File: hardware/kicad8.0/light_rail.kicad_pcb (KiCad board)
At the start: 4 copper layers, 73.4 x 100.5 mm, 215 parts, among them J1 USB_C_Receptacle_USB2.0_16P, J2 Conn_01x04_Pin, J3 AVR-ISP-6, SW1 SW_Push, SW10 SW_Push, SW11 SW_Push, SW12 SW_Push, SW13 SW_Push, SW14 SW_SPST, SW2 SW_Push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

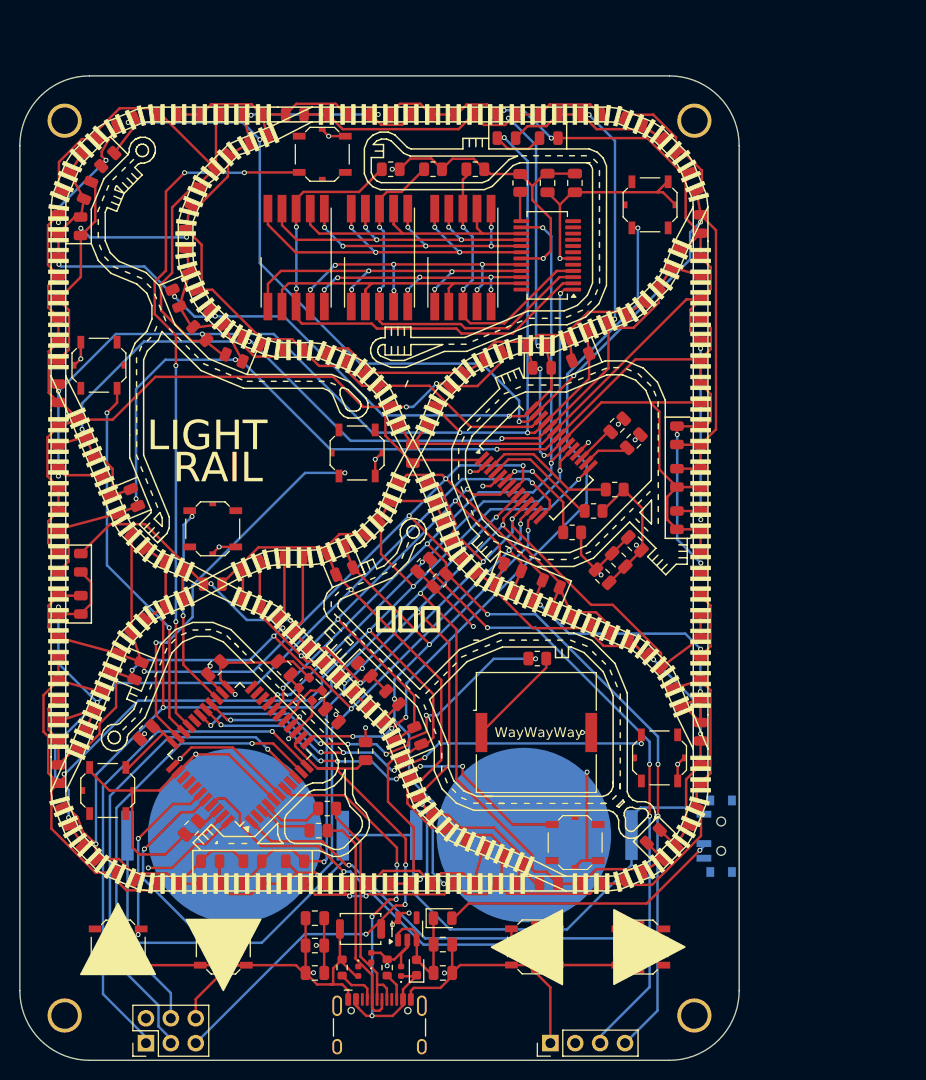
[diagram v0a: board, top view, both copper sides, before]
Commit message: added design comments to schematic, added schematic image
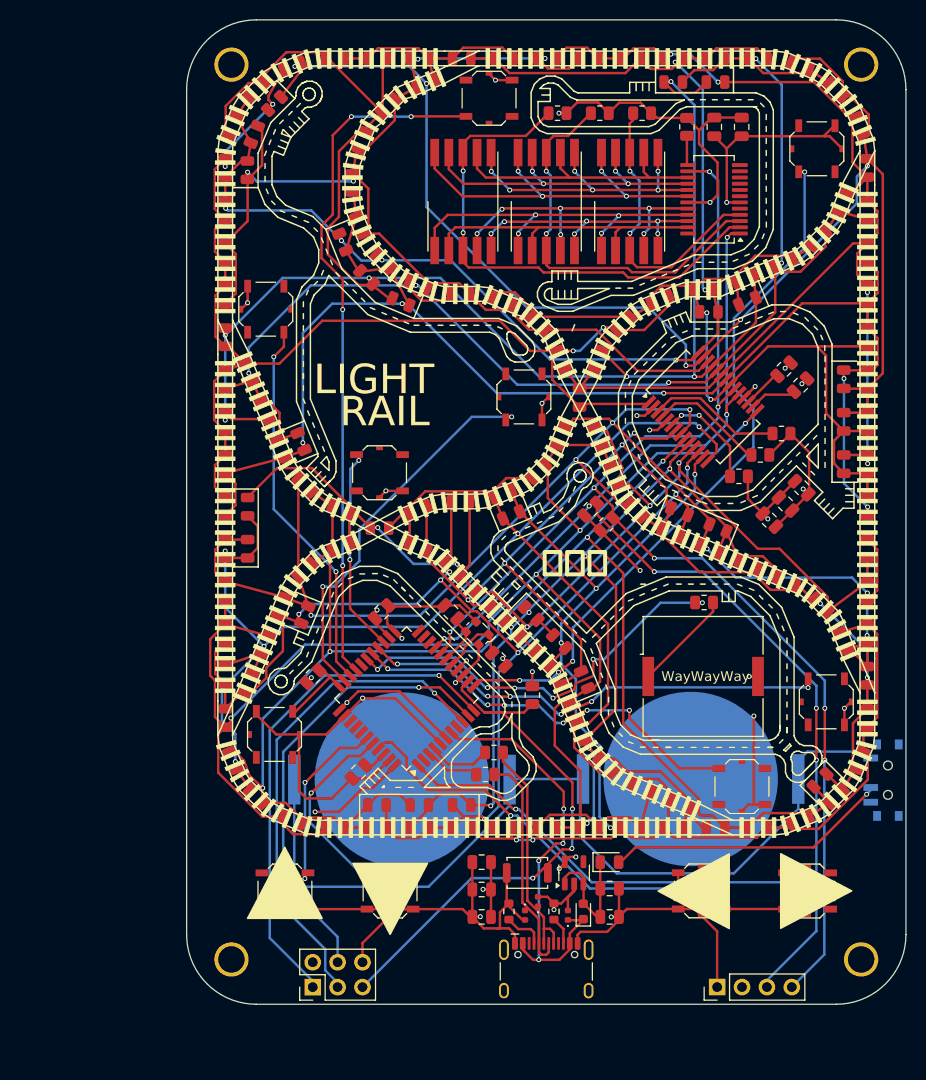
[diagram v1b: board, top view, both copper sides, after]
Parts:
- moved D130 18.0 mm to (74.3, 92.1)
- moved D134 18.0 mm to (64.6, 66.5)
- moved D136 18.0 mm to (72.1, 83.3)
- moved D76 18.0 mm to (88.8, 71.6)
- moved D78 18.0 mm to (81.8, 66.2)
- moved D81 18.0 mm to (70.1, 84.7)
- moved H4 18.0 mm to (100.3, 111.9)
- moved J2 18.0 mm to (85.6, 114.7)
- moved SW10 18.0 mm to (52.3, 104.9)
- moved SW12 18.0 mm to (94.9, 104.9)
- moved SW13 18.0 mm to (66.3, 103.0)
- moved SW8 18.0 mm to (88.2, 94.2)
- moved U4 18.0 mm to (71.0, 103.0)
- moved BT1 18.0 mm to (82.9, 93.5)
- moved BT2 18.0 mm to (53.5, 93.5)
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
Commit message: adding more images and moving around stuff
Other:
- board text removed: "WayWayWay"
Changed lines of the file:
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@@
-		)
-	)
-	(gr_text "WayWayWay"
-		(at 79.935301 83.586562 0)
-		(layer "F.SilkS")
-		(effects
-			(font
-				(size 1 1)
-				(thickness 0.1)
-			)
-			(justify left bottom)
 		)
 	)
